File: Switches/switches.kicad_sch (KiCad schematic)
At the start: 16 parts

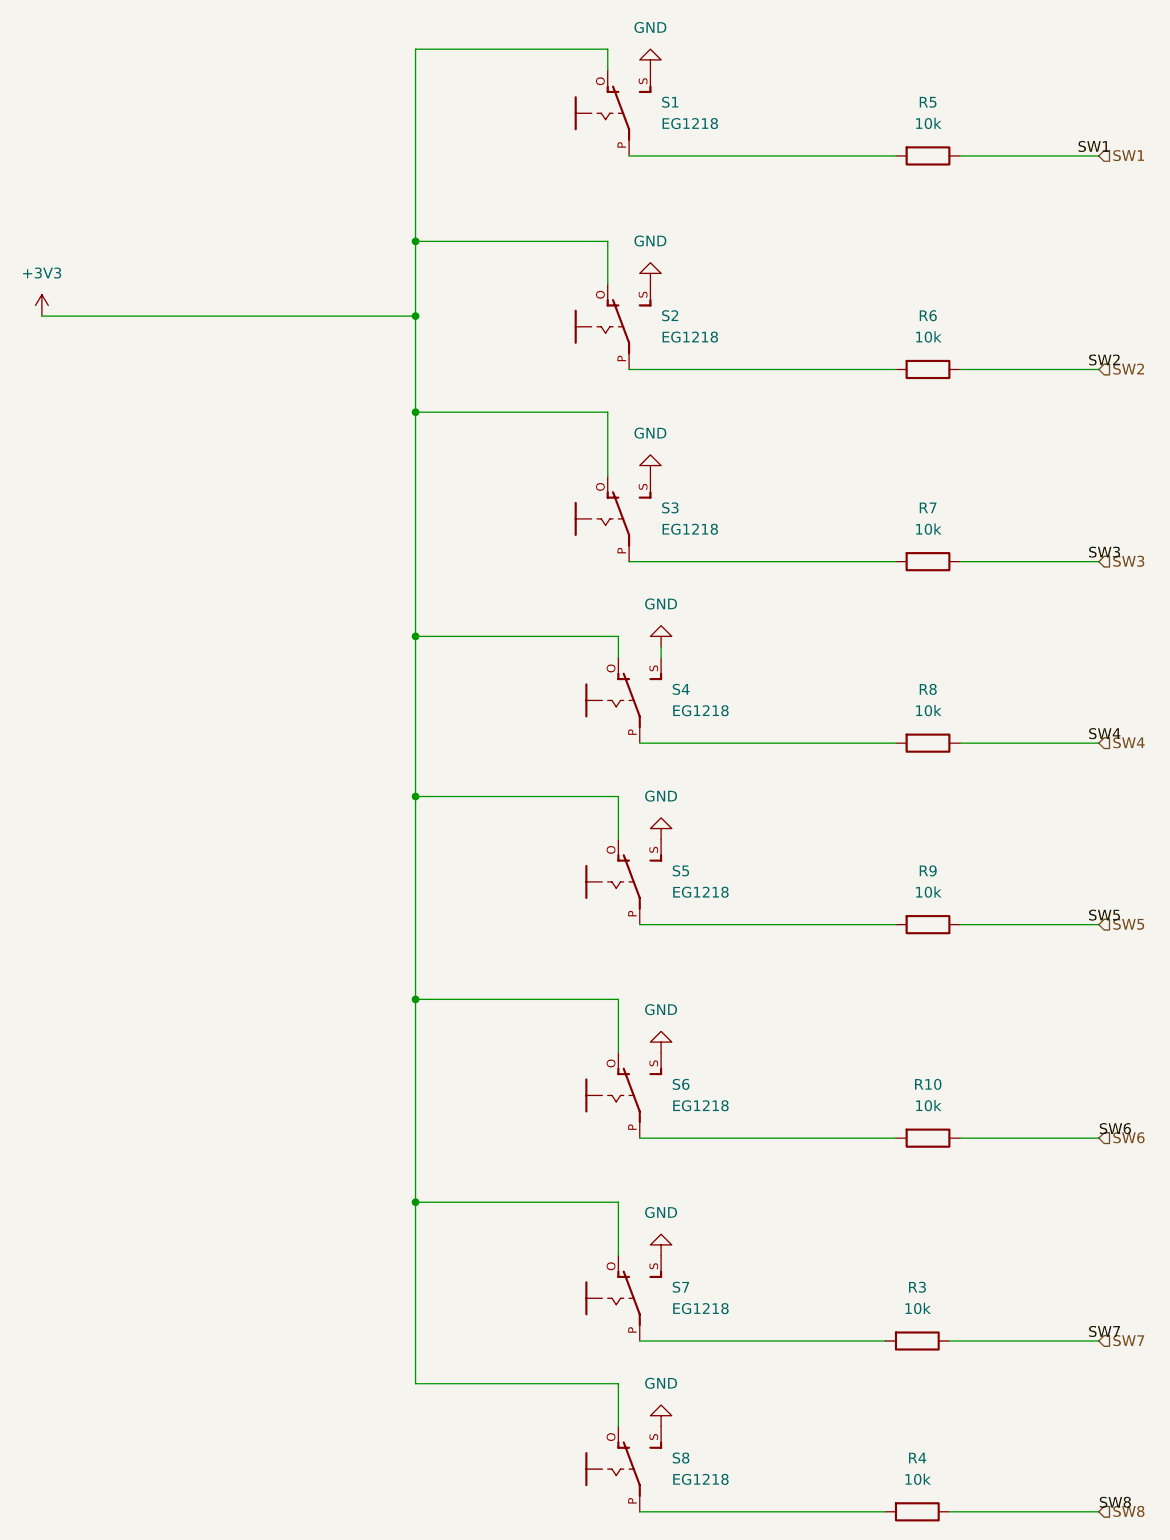
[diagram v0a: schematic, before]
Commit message: First week after winter break. Changed Power circuit design to use different DC to DC converter Setting correct footprints for the components like resistors and capacitors.
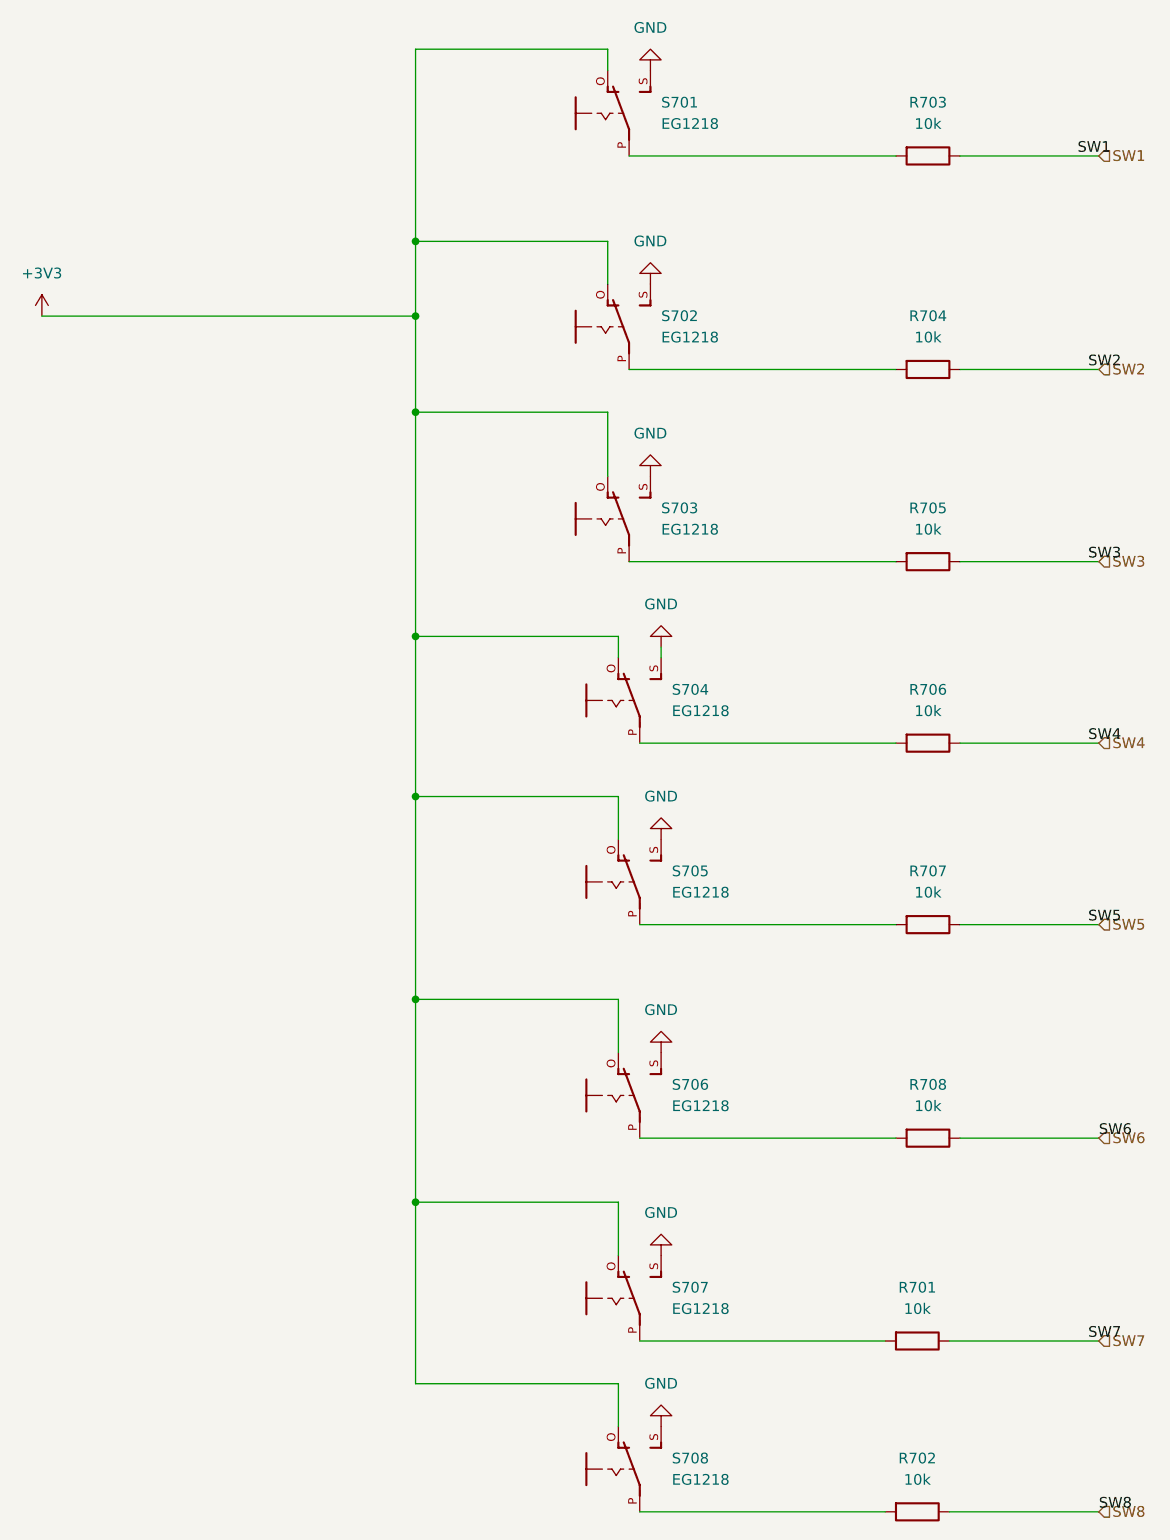
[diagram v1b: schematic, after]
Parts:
- R701: renamed from R3; footprint Resistor_SMD:R_0201_0603Metric -> Resistor_SMD:R_0603_1608Metric; Manufacturer_Name (none) -> UNI-ROYAL(Uniroyal Elec); Manufacturer_Part_Number (none) -> 0603WAF1002T5E
- R702: renamed from R4; footprint Resistor_SMD:R_0201_0603Metric -> Resistor_SMD:R_0603_1608Metric; Manufacturer_Name (none) -> UNI-ROYAL(Uniroyal Elec); Manufacturer_Part_Number (none) -> 0603WAF1002T5E
- R703: renamed from R5; footprint Resistor_SMD:R_0201_0603Metric -> Resistor_SMD:R_0603_1608Metric; Manufacturer_Name (none) -> UNI-ROYAL(Uniroyal Elec); Manufacturer_Part_Number (none) -> 0603WAF1002T5E
- R704: renamed from R6; footprint Resistor_SMD:R_0201_0603Metric -> Resistor_SMD:R_0603_1608Metric; Manufacturer_Name (none) -> UNI-ROYAL(Uniroyal Elec); Manufacturer_Part_Number (none) -> 0603WAF1002T5E
- R705: renamed from R7; footprint Resistor_SMD:R_0201_0603Metric -> Resistor_SMD:R_0603_1608Metric; Manufacturer_Name (none) -> UNI-ROYAL(Uniroyal Elec); Manufacturer_Part_Number (none) -> 0603WAF1002T5E
- R706: renamed from R8; footprint Resistor_SMD:R_0201_0603Metric -> Resistor_SMD:R_0603_1608Metric; Manufacturer_Name (none) -> UNI-ROYAL(Uniroyal Elec); Manufacturer_Part_Number (none) -> 0603WAF1002T5E
- R707: renamed from R9; footprint Resistor_SMD:R_0201_0603Metric -> Resistor_SMD:R_0603_1608Metric; Manufacturer_Name (none) -> UNI-ROYAL(Uniroyal Elec); Manufacturer_Part_Number (none) -> 0603WAF1002T5E
- R708: renamed from R10; footprint Resistor_SMD:R_0201_0603Metric -> Resistor_SMD:R_0603_1608Metric; Manufacturer_Name (none) -> UNI-ROYAL(Uniroyal Elec); Manufacturer_Part_Number (none) -> 0603WAF1002T5E
- S707: renamed from S7; footprint Custom:EG1218 -> EG1218
- renumbered S1 to S701, S2 to S702, S3 to S703, S4 to S704, S5 to S705, S6 to S706, S8 to S708

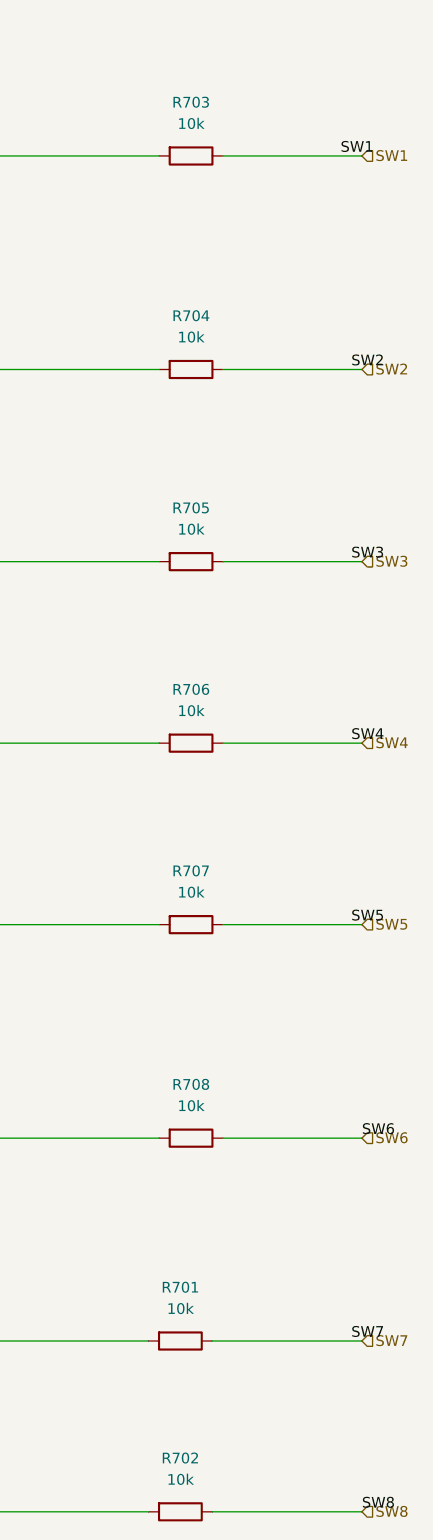
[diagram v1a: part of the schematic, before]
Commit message: Weekend progress
Things that remain:
4 LEDs to Microcontroller
7-Seg to Microcontroller
LCD to Microcontroller
Microphone and Speakers to Microcontroller
Power circuitry
USB-C connector
Reset and Boot buttons
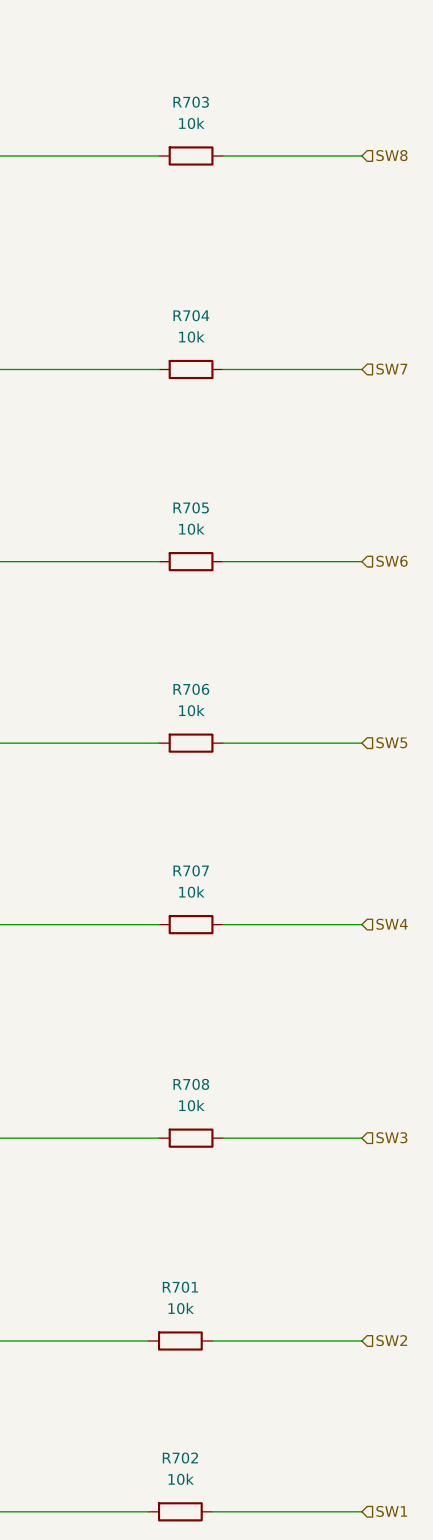
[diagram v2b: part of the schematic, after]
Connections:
- net SW1: now also R702.1; no longer R703.1
- net SW2: now also R701.1; no longer R704.1
- net SW3: now also R708.1; no longer R705.1
- net SW4: now also R707.1; no longer R706.1
- net SW5: now also R706.1; no longer R707.1
- net SW6: now also R705.1; no longer R708.1
- net SW7: now also R704.1; no longer R701.1
- net SW8: now also R703.1; no longer R702.1
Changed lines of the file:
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@@
     (stroke (width 0) (type default) (color 0 0 0 0))
   )
-  (label "SW3" (at 153.67 77.47 0)
-    (effects (font (size 1.27 1.27)) (justify left bottom))
-  )
-  (label "SW6" (at 154.94 146.05 0)
-    (effects (font (size 1.27 1.27)) (justify left bottom))
-  )
-  (label "SW5" (at 153.67 120.65 0)
-    (effects (font (size 1.27 1.27)) (justify left bottom))
-  )
-  (label "SW2" (at 153.67 54.61 0)
-    (effects (font (size 1.27 1.27)) (justify left bottom))
-  )
-  (label "SW8" (at 154.94 190.5 0)
-    (effects (font (size 1.27 1.27)) (justify left bottom))
-  )
-  (label "SW1" (at 152.4 29.21 0)
-    (effects (font (size 1.27 1.27)) (justify left bottom))
-  )
-  (label "SW7" (at 153.67 170.18 0)
-    (effects (font (size 1.27 1.27)) (justify left bottom))
-  )
-  (label "SW4" (at 153.67 99.06 0)
-    (effects (font (size 1.27 1.27)) (justify left bottom))
-  )
-  (hierarchical_label "SW4" (shape input) (at 154.94 99.06 0)
+  (hierarchical_label "SW5" (shape input) (at 154.94 99.06 0)
     (effects (font (size 1.27 1.27)) (justify left))
   )
-  (hierarchical_label "SW5" (shape input) (at 154.94 120.65 0)
+  (hierarchical_label "SW4" (shape input) (at 154.94 120.65 0)
     (effects (font (size 1.27 1.27)) (justify left))
   )
-  (hierarchical_label "SW3" (shape input) (at 154.94 77.47 0)
+  (hierarchical_label "SW6" (shape input) (at 154.94 77.47 0)
     (effects (font (size 1.27 1.27)) (justify left))
   )
-  (hierarchical_label "SW7" (shape input) (at 154.94 170.18 0)
+  (hierarchical_label "SW2" (shape input) (at 154.94 170.18 0)
     (effects (font (size 1.27 1.27)) (justify left))
   )
-  (hierarchical_label "SW8" (shape input) (at 154.94 190.5 0)
+  (hierarchical_label "SW1" (shape input) (at 154.94 190.5 0)
     (effects (font (size 1.27 1.27)) (justify left))
   )
-  (hierarchical_label "SW6" (shape input) (at 154.94 146.05 0)
+  (hierarchical_label "SW3" (shape input) (at 154.94 146.05 0)
     (effects (font (size 1.27 1.27)) (justify left))
   )
-  (hierarchical_label "SW1" (shape input) (at 154.94 29.21 0)
+  (hierarchical_label "SW8" (shape input) (at 154.94 29.21 0)
     (effects (font (size 1.27 1.27)) (justify left))
   )
-  (hierarchical_label "SW2" (shape input) (at 154.94 54.61 0)
+  (hierarchical_label "SW7" (shape input) (at 154.94 54.61 0)
     (effects (font (size 1.27 1.27)) (justify left))
   )

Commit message: REVISION 0 DONE
Done first revision of the UDUINO
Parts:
- renumbered R703 to R701, R704 to R702, R705 to R703, R706 to R704, R707 to R705, R708 to R706, R701 to R707, R702 to R708
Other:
- moved on the sheet: R707, R708
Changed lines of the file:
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@@
     (stroke (width 0) (type default) (color 0 0 0 0))
   )
-  (wire (pts (xy 137.16 170.18) (xy 154.94 170.18))
+  (wire (pts (xy 138.43 170.18) (xy 154.94 170.18))
     (stroke (width 0) (type default) (color 0 0 0 0))
   )
@@
     (stroke (width 0) (type default) (color 0 0 0 0))
   )
-  (wire (pts (xy 137.16 190.5) (xy 154.94 190.5))
+  (wire (pts (xy 138.43 190.5) (xy 154.94 190.5))
     (stroke (width 0) (type default) (color 0 0 0 0))
   )
@@
     (stroke (width 0) (type default) (color 0 0 0 0))
   )
-  (wire (pts (xy 100.33 170.18) (xy 129.54 170.18))
+  (wire (pts (xy 100.33 170.18) (xy 130.81 170.18))
     (stroke (width 0) (type default) (color 0 0 0 0))
   )
@@
     (stroke (width 0) (type default) (color 0 0 0 0))
   )
-  (wire (pts (xy 100.33 190.5) (xy 129.54 190.5))
+  (wire (pts (xy 100.33 190.5) (xy 130.81 190.5))
     (stroke (width 0) (type default) (color 0 0 0 0))
   )
@@
   (symbol (lib_id "Device:R") (at 134.62 29.21 270) (unit 1)
     (in_bom yes) (on_board yes) (fields_autoplaced)
-    (property "Reference" "R703" (id 0) (at 134.62 22.86 90))
+    (property "Reference" "R701" (id 0) (at 134.62 22.86 90))
     (property "Value" "10k" (id 1) (at 134.62 25.4 90))
     (property "Footprint" "Resistor_SMD:R_0603_1608Metric" (id 2) (at 134.62 27.432 90)
@@
   (symbol (lib_id "Device:R") (at 134.62 120.65 270) (unit 1)
     (in_bom yes) (on_board yes) (fields_autoplaced)
-    (property "Reference" "R707" (id 0) (at 134.62 114.3 90))
+    (property "Reference" "R705" (id 0) (at 134.62 114.3 90))
     (property "Value" "10k" (id 1) (at 134.62 116.84 90))
     (property "Footprint" "Resistor_SMD:R_0603_1608Metric" (id 2) (at 134.62 118.872 90)
@@
   (symbol (lib_id "Device:R") (at 134.62 99.06 270) (unit 1)
     (in_bom yes) (on_board yes) (fields_autoplaced)
-    (property "Reference" "R706" (id 0) (at 134.62 92.71 90))
+    (property "Reference" "R704" (id 0) (at 134.62 92.71 90))
     (property "Value" "10k" (id 1) (at 134.62 95.25 90))
     (property "Footprint" "Resistor_SMD:R_0603_1608Metric" (id 2) (at 134.62 97.282 90)
@@
   (symbol (lib_id "Device:R") (at 134.62 54.61 270) (unit 1)
     (in_bom yes) (on_board yes) (fields_autoplaced)
-    (property "Reference" "R704" (id 0) (at 134.62 48.26 90))
+    (property "Reference" "R702" (id 0) (at 134.62 48.26 90))
     (property "Value" "10k" (id 1) (at 134.62 50.8 90))
     (property "Footprint" "Resistor_SMD:R_0603_1608Metric" (id 2) (at 134.62 52.832 90)
@@
   (symbol (lib_id "Device:R") (at 134.62 77.47 270) (unit 1)
     (in_bom yes) (on_board yes) (fields_autoplaced)
-    (property "Reference" "R705" (id 0) (at 134.62 71.12 90))
+    (property "Reference" "R703" (id 0) (at 134.62 71.12 90))
     (property "Value" "10k" (id 1) (at 134.62 73.66 90))
     (property "Footprint" "Resistor_SMD:R_0603_1608Metric" (id 2) (at 134.62 75.692 90)
@@
     (pin "1")
   )
-  (symbol (lib_id "Device:R") (at 133.35 170.18 270) (unit 1)
-    (in_bom yes) (on_board yes) (fields_autoplaced)
-    (property "Reference" "R701" (id 0) (at 133.35 163.83 90))
-    (property "Value" "10k" (id 1) (at 133.35 166.37 90))
-    (property "Footprint" "Resistor_SMD:R_0603_1608Metric" (id 2) (at 133.35 168.402 90)
-      (effects (font (size 1.27 1.27)) hide)
-    )
-    (property "Datasheet" "~" (id 3) (at 133.35 170.18 0)
-      (effects (font (size 1.27 1.27)) hide)
-    )
-    (property "Manufacturer_Name" "UNI-ROYAL(Uniroyal Elec)" (id 4) (at 133.35 170.18 0)
-      (effects (font (size 1.27 1.27)) hide)
-    )
-    (property "Manufacturer_Part_Number" "0603WAF1002T5E" (id 5) (at 133.35 170.18 0)
+  (symbol (lib_id "Device:R") (at 134.62 170.18 270) (unit 1)
+    (in_bom yes) (on_board yes) (fields_autoplaced)
+    (property "Reference" "R707" (id 0) (at 134.62 163.83 90))
+    (property "Value" "10k" (id 1) (at 134.62 166.37 90))
+    (property "Footprint" "Resistor_SMD:R_0603_1608Metric" (id 2) (at 134.62 168.402 90)
+      (effects (font (size 1.27 1.27)) hide)
+    )
+    (property "Datasheet" "~" (id 3) (at 134.62 170.18 0)
+      (effects (font (size 1.27 1.27)) hide)
+    )
+    (property "Manufacturer_Name" "UNI-ROYAL(Uniroyal Elec)" (id 4) (at 134.62 170.18 0)
+      (effects (font (size 1.27 1.27)) hide)
+    )
+    (property "Manufacturer_Part_Number" "0603WAF1002T5E" (id 5) (at 134.62 170.18 0)
       (effects (font (size 1.27 1.27)) hide)
     )
@@
     (pin "1")
   )
-  (symbol (lib_id "Device:R") (at 133.35 190.5 270) (unit 1)
-    (in_bom yes) (on_board yes) (fields_autoplaced)
-    (property "Reference" "R702" (id 0) (at 133.35 184.15 90))
-    (property "Value" "10k" (id 1) (at 133.35 186.69 90))
-    (property "Footprint" "Resistor_SMD:R_0603_1608Metric" (id 2) (at 133.35 188.722 90)
-      (effects (font (size 1.27 1.27)) hide)
-    )
-    (property "Datasheet" "~" (id 3) (at 133.35 190.5 0)
-      (effects (font (size 1.27 1.27)) hide)
-    )
-    (property "Manufacturer_Name" "UNI-ROYAL(Uniroyal Elec)" (id 4) (at 133.35 190.5 0)
-      (effects (font (size 1.27 1.27)) hide)
-    )
-    (property "Manufacturer_Part_Number" "0603WAF1002T5E" (id 5) (at 133.35 190.5 0)
+  (symbol (lib_id "Device:R") (at 134.62 190.5 270) (unit 1)
+    (in_bom yes) (on_board yes) (fields_autoplaced)
+    (property "Reference" "R708" (id 0) (at 134.62 184.15 90))
+    (property "Value" "10k" (id 1) (at 134.62 186.69 90))
+    (property "Footprint" "Resistor_SMD:R_0603_1608Metric" (id 2) (at 134.62 188.722 90)
+      (effects (font (size 1.27 1.27)) hide)
+    )
+    (property "Datasheet" "~" (id 3) (at 134.62 190.5 0)
+      (effects (font (size 1.27 1.27)) hide)
+    )
+    (property "Manufacturer_Name" "UNI-ROYAL(Uniroyal Elec)" (id 4) (at 134.62 190.5 0)
+      (effects (font (size 1.27 1.27)) hide)
+    )
+    (property "Manufacturer_Part_Number" "0603WAF1002T5E" (id 5) (at 134.62 190.5 0)
       (effects (font (size 1.27 1.27)) hide)
     )
@@
   (symbol (lib_id "Device:R") (at 134.62 146.05 270) (unit 1)
     (in_bom yes) (on_board yes) (fields_autoplaced)
-    (property "Reference" "R708" (id 0) (at 134.62 139.7 90))
+    (property "Reference" "R706" (id 0) (at 134.62 139.7 90))
     (property "Value" "10k" (id 1) (at 134.62 142.24 90))
     (property "Footprint" "Resistor_SMD:R_0603_1608Metric" (id 2) (at 134.62 144.272 90)
